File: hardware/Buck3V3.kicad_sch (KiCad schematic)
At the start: 10 parts, among them U301 AP63203WU

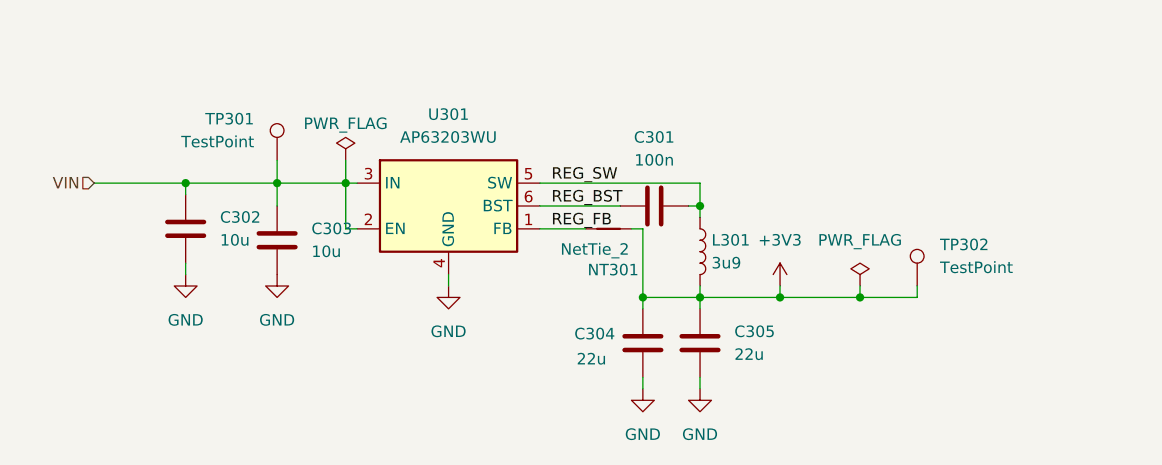
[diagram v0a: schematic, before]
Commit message: Optimized BOM and added netties
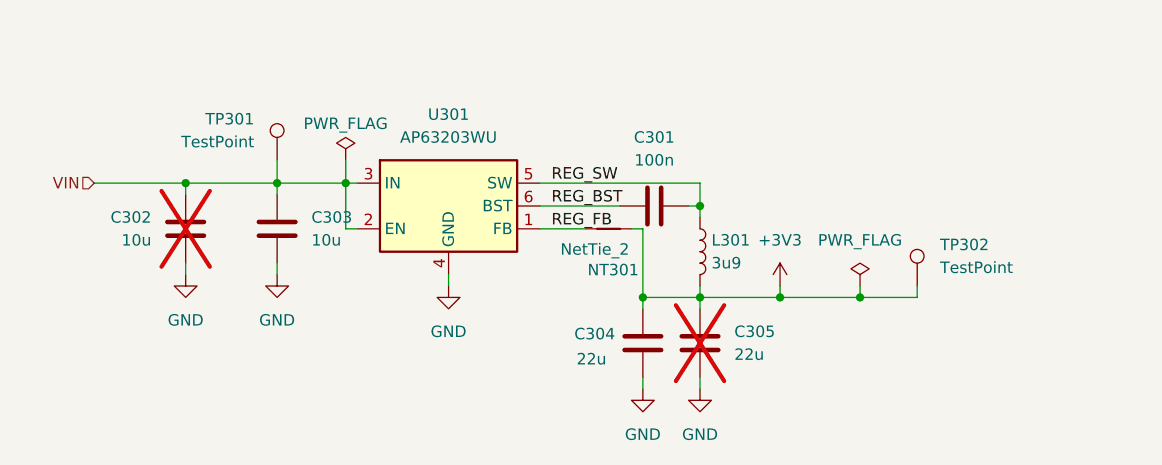
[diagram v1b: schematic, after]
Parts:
- C302, C305: now not fitted
- NT301: footprint rise:NETTIE_0.3mm -> glowbuck:NETTIE_0.3mm
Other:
- moved on the sheet: C303
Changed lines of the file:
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@@
 	(wire
 		(pts
-			(xy 53.34 48.26) (xy 53.34 45.72)
+			(xy 53.34 46.99) (xy 53.34 45.72)
 		)
 		(stroke
@@
 		(pts
 			(xy 118.11 58.42) (xy 118.11 57.15)
+		)
+		(stroke
+			(width 0)
+			(type default)
+		)
+	)
+	(wire
+		(pts
+			(xy 53.34 54.61) (xy 53.34 55.88)
 		)
 		(stroke
@@
 		(in_bom yes)
 		(on_board yes)
-		(dnp no)
+		(dnp yes)
 		(fields_autoplaced yes)
 		(property "Reference" "C302"
-			(at 46.99 49.5299 0)
-			(effects
-				(font
-					(size 1.27 1.27)
-				)
-				(justify left)
+			(at 39.37 49.5299 0)
+			(effects
+				(font
+					(size 1.27 1.27)
+				)
+				(justify right)
 			)
 		)
 		(property "Value" "10u"
-			(at 46.99 52.0699 0)
-			(effects
-				(font
-					(size 1.27 1.27)
-				)
-				(justify left)
+			(at 39.37 52.0699 0)
+			(effects
+				(font
+					(size 1.27 1.27)
+				)
+				(justify right)
 			)
 		)
@@
 	(symbol
 		(lib_id "Device:C")
-		(at 53.34 52.07 180)
+		(at 53.34 50.8 180)
 		(unit 1)
 		(exclude_from_sim no)
@@
 		(fields_autoplaced yes)
 		(property "Reference" "C303"
-			(at 57.15 50.7999 0)
+			(at 57.15 49.5299 0)
 			(effects
 				(font
@@
 		)
 		(property "Value" "10u"
-			(at 57.15 53.3399 0)
+			(at 57.15 52.0699 0)
 			(effects
 				(font
@@
 		)
 		(property "Footprint" "Capacitor_SMD:C_1210_3225Metric_Pad1.33x2.70mm_HandSolder"
-			(at 52.3748 48.26 0)
+			(at 52.3748 46.99 0)
 			(effects
 				(font
@@
 		)
 		(property "Datasheet" "~"
-			(at 53.34 52.07 0)
+			(at 53.34 50.8 0)
 			(effects
 				(font
@@
 		)
 		(property "Description" "Unpolarized capacitor"
-			(at 53.34 52.07 0)
+			(at 53.34 50.8 0)
 			(effects
 				(font
@@
 		)
 		(property "Sim.Device" ""
-			(at 53.34 52.07 0)
+			(at 53.34 50.8 0)
 			(effects
 				(font
@@
 		)
 		(property "Sim.Type" ""
-			(at 53.34 52.07 0)
+			(at 53.34 50.8 0)
 			(effects
 				(font
@@
 		)
 		(property "MouserNumber" "187-CL32B106KBJNNNE"
-			(at 53.34 52.07 0)
+			(at 53.34 50.8 0)
 			(effects
 				(font
@@
 		)
 		(property "OrderLink" ""
-			(at 53.34 52.07 0)
+			(at 53.34 50.8 0)
 			(effects
 				(font
@@
 		)
 		(property "Qty" ""
-			(at 53.34 52.07 0)
+			(at 53.34 50.8 0)
 			(effects
 				(font
@@
 		(in_bom yes)
 		(on_board yes)
-		(dnp no)
+		(dnp yes)
 		(fields_autoplaced yes)
 		(property "Reference" "C305"
@@
 			)
 		)
-		(property "Footprint" "rise:NETTIE_0.3mm"
+		(property "Footprint" "glowbuck:NETTIE_0.3mm"
 			(at 90.17 50.8 0)
 			(effects

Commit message: Changed footprints to non hand solder option
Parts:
- C301: footprint Capacitor_SMD:C_0603_1608Metric_Pad1.08x0.95mm_HandSolder -> Capacitor_SMD:C_0603_1608Metric
- C302, C303: footprint Capacitor_SMD:C_1210_3225Metric_Pad1.33x2.70mm_HandSolder -> Capacitor_SMD:C_1210_3225Metric
- C304, C305: footprint Capacitor_SMD:C_0805_2012Metric_Pad1.18x1.45mm_HandSolder -> Capacitor_SMD:C_0805_2012Metric
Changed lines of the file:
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@@
 			)
 		)
-		(property "Footprint" "Capacitor_SMD:C_1210_3225Metric_Pad1.33x2.70mm_HandSolder"
+		(property "Footprint" "Capacitor_SMD:C_1210_3225Metric"
 			(at 44.1452 54.61 0)
 			(effects
@@
 			)
 		)
-		(property "Footprint" "Capacitor_SMD:C_1210_3225Metric_Pad1.33x2.70mm_HandSolder"
+		(property "Footprint" "Capacitor_SMD:C_1210_3225Metric"
 			(at 52.3748 46.99 0)
 			(effects
@@
 			)
 		)
-		(property "Footprint" "Capacitor_SMD:C_0603_1608Metric_Pad1.08x0.95mm_HandSolder"
+		(property "Footprint" "Capacitor_SMD:C_0603_1608Metric"
 			(at 99.06 47.2948 0)
 			(effects
@@
 			)
 		)
-		(property "Footprint" "Capacitor_SMD:C_0805_2012Metric_Pad1.18x1.45mm_HandSolder"
+		(property "Footprint" "Capacitor_SMD:C_0805_2012Metric"
 			(at 99.3648 59.69 0)
 			(effects
@@
 			)
 		)
-		(property "Footprint" "Capacitor_SMD:C_0805_2012Metric_Pad1.18x1.45mm_HandSolder"
+		(property "Footprint" "Capacitor_SMD:C_0805_2012Metric"
 			(at 93.0148 59.69 0)
 			(effects

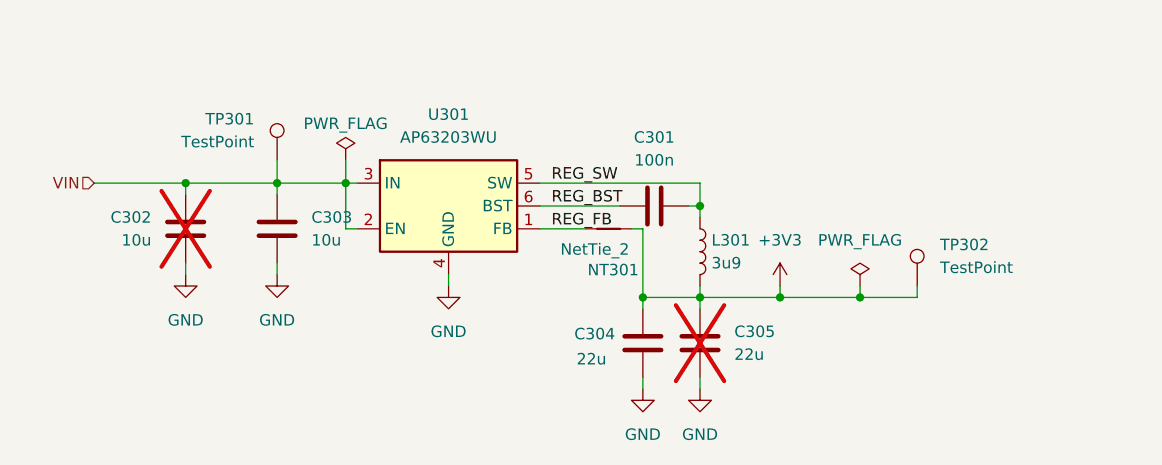
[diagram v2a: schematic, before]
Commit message: Colored nets and added optional current measurement
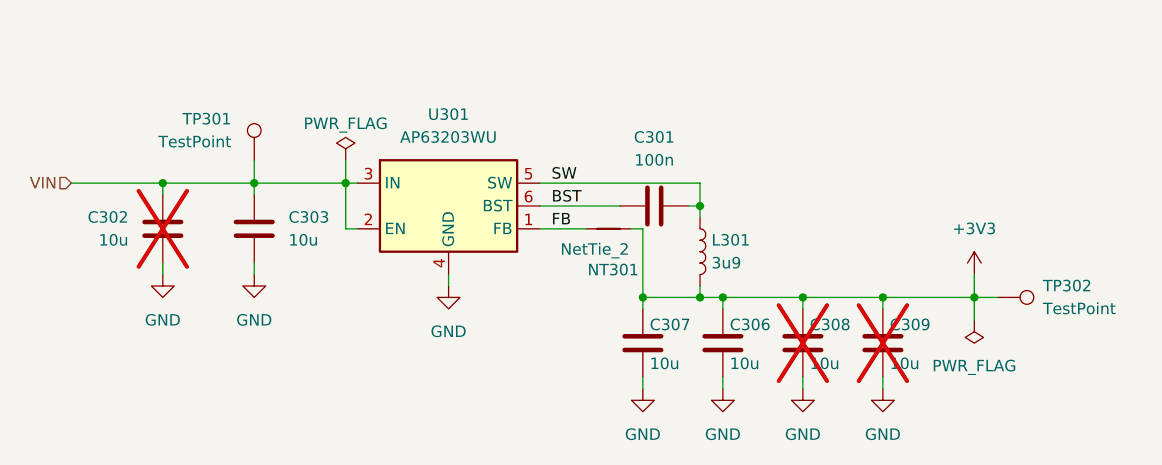
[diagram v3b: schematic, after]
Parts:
- removed C304, C305: 22u, Capacitor_SMD:C_0805_2012Metric, symbol Device:C
- added C306, C307, C308, C309: 10u, Capacitor_SMD:C_0603_1608Metric, symbol Device:C
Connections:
- net +3V3: now also C306.2, C307.2, C308.2, C309.2
- net GND: now also C306.1, C307.1, C308.1, C309.1
- net REG_BST renamed BST
- net REG_FB renamed FB
- net REG_SW renamed SW
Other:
- moved on the sheet: C302, C303, TP301, TP302

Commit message: Global labels, explanation texts, fix spring connector
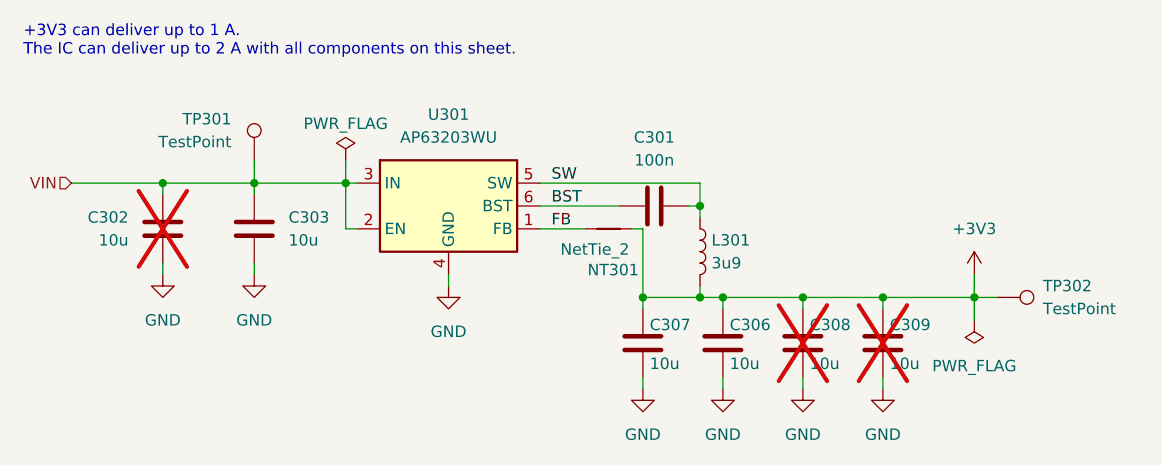
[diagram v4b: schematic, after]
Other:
- note added: "+3V3 can deliver up to 1 A. The IC can deliver up to 2 A with all components on this sheet."
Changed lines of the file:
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@@
 		(title "Glowbuck")
+	)
+	(text "+3V3 can deliver up to 1 A.\nThe IC can deliver up to 2 A with all components on this sheet."
+		(exclude_from_sim no)
+		(at 25.146 28.194 0)
+		(effects
+			(font
+				(size 1.27 1.27)
+			)
+			(justify left top)
+		)
 	)
 	(junction

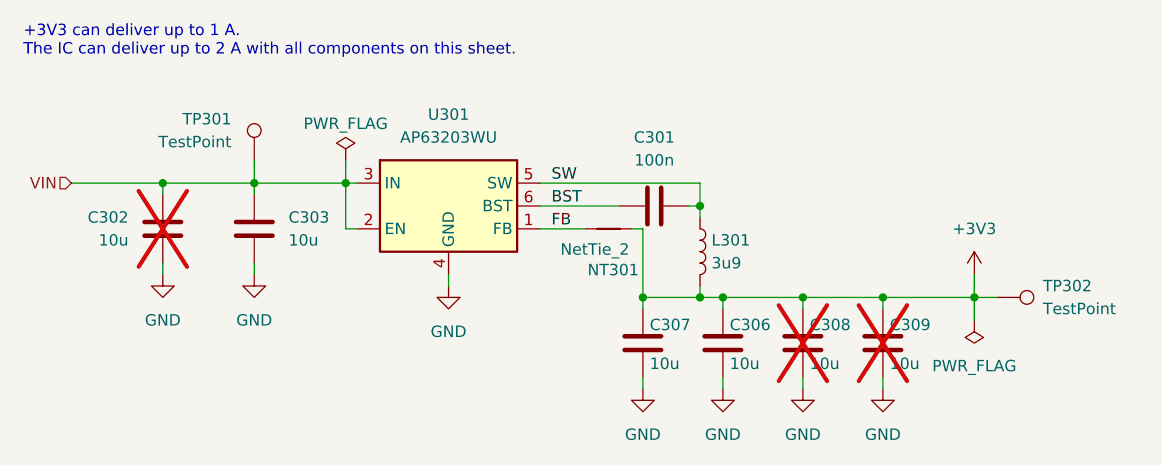
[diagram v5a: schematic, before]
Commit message: Layout in progress. I2C done
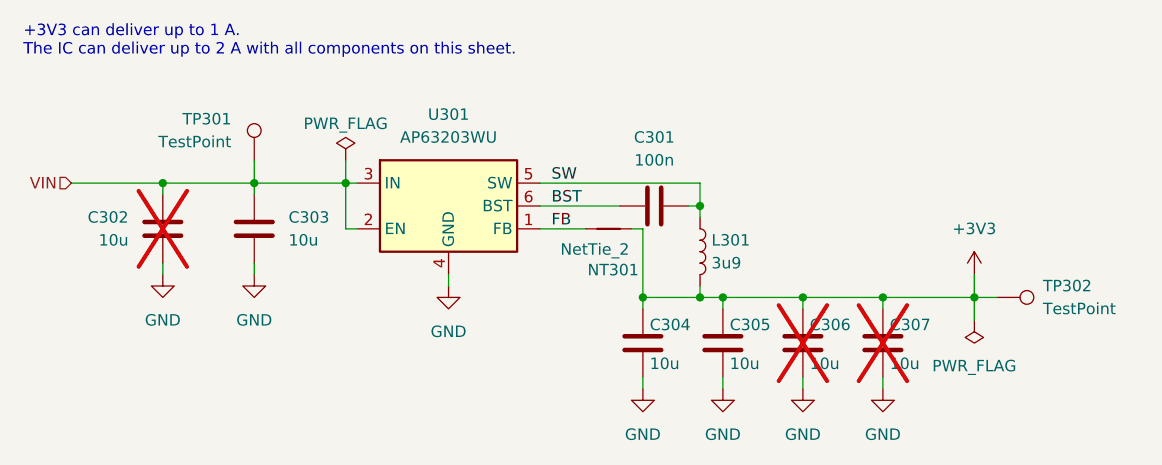
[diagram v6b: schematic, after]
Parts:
- renumbered C307 to C304, C306 to C305, C308 to C306, C309 to C307
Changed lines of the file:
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@@
 		(dnp no)
 		(fields_autoplaced yes)
-		(property "Reference" "#PWR0309"
+		(property "Reference" "#PWR0308"
 			(at 120.65 74.93 0)
 			(effects
@@
 			(project "glowbuck"
 				(path "/5c22e6dd-0c33-4422-b6db-bb3ef40a8534/4d6386b4-aba2-4d32-a7eb-dee692c742f8"
-					(reference "#PWR0309")
+					(reference "#PWR0308")
 					(unit 1)
 				)
@@
 		(exclude_from_sim no)
 		(in_bom yes)
-		(on_board yes)
+		(on_board no)
 		(dnp yes)
 		(fields_autoplaced yes)
@@
 		(on_board yes)
 		(dnp no)
-		(property "Reference" "C306"
+		(property "Reference" "C305"
 			(at 103.632 61.468 0)
 			(effects
@@
 			(project "glowbuck"
 				(path "/5c22e6dd-0c33-4422-b6db-bb3ef40a8534/4d6386b4-aba2-4d32-a7eb-dee692c742f8"
-					(reference "C306")
+					(reference "C305")
 					(unit 1)
 				)
@@
 		(exclude_from_sim no)
 		(in_bom yes)
-		(on_board yes)
+		(on_board no)
 		(dnp yes)
-		(property "Reference" "C308"
+		(property "Reference" "C306"
 			(at 112.522 61.468 0)
 			(effects
@@
 			(project "glowbuck"
 				(path "/5c22e6dd-0c33-4422-b6db-bb3ef40a8534/4d6386b4-aba2-4d32-a7eb-dee692c742f8"
-					(reference "C308")
+					(reference "C306")
 					(unit 1)
 				)
@@
 		(exclude_from_sim no)
 		(in_bom yes)
-		(on_board yes)
+		(on_board no)
 		(dnp yes)
-		(property "Reference" "C309"
+		(property "Reference" "C307"
 			(at 121.412 61.468 0)
 			(effects
@@
 			(project "glowbuck"
 				(path "/5c22e6dd-0c33-4422-b6db-bb3ef40a8534/4d6386b4-aba2-4d32-a7eb-dee692c742f8"
-					(reference "C309")
+					(reference "C307")
 					(unit 1)
 				)
@@
 		(dnp no)
 		(fields_autoplaced yes)
-		(property "Reference" "#PWR0307"
+		(property "Reference" "#PWR0306"
 			(at 102.87 74.93 0)
 			(effects
@@
 			(project "glowbuck"
 				(path "/5c22e6dd-0c33-4422-b6db-bb3ef40a8534/4d6386b4-aba2-4d32-a7eb-dee692c742f8"
-					(reference "#PWR0307")
+					(reference "#PWR0306")
 					(unit 1)
 				)
@@
 		(dnp no)
 		(fields_autoplaced yes)
-		(property "Reference" "#PWR0303"
+		(property "Reference" "#PWR0304"
 			(at 72.39 63.5 0)
 			(effects
@@
 			(project "glowbuck"
 				(path "/5c22e6dd-0c33-4422-b6db-bb3ef40a8534/4d6386b4-aba2-4d32-a7eb-dee692c742f8"
-					(reference "#PWR0303")
+					(reference "#PWR0304")
 					(unit 1)
 				)
@@
 		(dnp no)
 		(fields_autoplaced yes)
-		(property "Reference" "#PWR0308"
+		(property "Reference" "#PWR0307"
 			(at 111.76 74.93 0)
 			(effects
@@
 			(project "glowbuck"
 				(path "/5c22e6dd-0c33-4422-b6db-bb3ef40a8534/4d6386b4-aba2-4d32-a7eb-dee692c742f8"
-					(reference "#PWR0308")
+					(reference "#PWR0307")
 					(unit 1)
 				)
@@
 		(dnp no)
 		(fields_autoplaced yes)
-		(property "Reference" "#PWR0304"
+		(property "Reference" "#PWR0303"
 			(at 130.81 59.69 0)
 			(effects
@@
 			(project "glowbuck"
 				(path "/5c22e6dd-0c33-4422-b6db-bb3ef40a8534/4d6386b4-aba2-4d32-a7eb-dee692c742f8"
-					(reference "#PWR0304")
+					(reference "#PWR0303")
 					(unit 1)
 				)
@@
 		(on_board yes)
 		(dnp no)
-		(property "Reference" "C307"
+		(property "Reference" "C304"
 			(at 94.742 61.468 0)
 			(effects
@@
 			(project "glowbuck"
 				(path "/5c22e6dd-0c33-4422-b6db-bb3ef40a8534/4d6386b4-aba2-4d32-a7eb-dee692c742f8"
-					(reference "C307")
-					(unit 1)
-				)
+					(reference "C304")
+					(unit 1)
+				)

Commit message: Added ManufacturerNumber for every item and fixed bom errors
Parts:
- C301: ManufacturerNumber (none) -> CL10B104KB8WPND
- C302, C303: ManufacturerNumber (none) -> CL32B106KBJNNNE
- C304, C305, C306, C307: ManufacturerNumber (none) -> CL10A106MA8NRNC
- L301: ManufacturerNumber (none) -> SRR7045-3R9M
- U301: ManufacturerNumber (none) -> AP63203WU-7
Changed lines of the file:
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@@
+			)
+		)
+		(property "ManufacturerNumber" "CL32B106KBJNNNE"
+			(at 40.64 50.8 0)
+			(effects
+				(font
+					(size 1.27 1.27)
+				)
+				(hide yes)
 			)
 		)
@@
 		)
 		(property "Part" ""
+			(at 102.87 63.5 0)
+			(effects
+				(font
+					(size 1.27 1.27)
+				)
+				(hide yes)
+			)
+		)
+		(property "ManufacturerNumber" "CL10A106MA8NRNC"
 			(at 102.87 63.5 0)
 			(effects
@@
 			)
 		)
+		(property "ManufacturerNumber" "CL32B106KBJNNNE"
+			(at 50.8 50.8 0)
+			(effects
+				(font
+					(size 1.27 1.27)
+				)
+				(hide yes)
+			)
+		)
 		(pin "2"
 		)
@@
 			)
 		)
+		(property "ManufacturerNumber" "CL10A106MA8NRNC"
+			(at 111.76 63.5 0)
+			(effects
+				(font
+					(size 1.27 1.27)
+				)
+				(hide yes)
+			)
+		)
 		(pin "2"
 		)
@@
 		)
 		(property "Part" ""
+			(at 120.65 63.5 0)
+			(effects
+				(font
+					(size 1.27 1.27)
+				)
+				(hide yes)
+			)
+		)
+		(property "ManufacturerNumber" "CL10A106MA8NRNC"
 			(at 120.65 63.5 0)
 			(effects
@@
 			)
 		)
+		(property "ManufacturerNumber" "AP63203WU-7"
+			(at 72.39 48.26 0)
+			(effects
+				(font
+					(size 1.27 1.27)
+				)
+				(hide yes)
+			)
+		)
 		(pin "4"
 		)
@@
 		)
 		(property "Part" ""
+			(at 100.33 53.34 0)
+			(effects
+				(font
+					(size 1.27 1.27)
+				)
+				(hide yes)
+			)
+		)
+		(property "ManufacturerNumber" "SRR7045-3R9M"
 			(at 100.33 53.34 0)
 			(effects
@@
 			)
 		)
+		(property "ManufacturerNumber" "CL10B104KB8WPND"
+			(at 95.25 48.26 90)
+			(effects
+				(font
+					(size 1.27 1.27)
+				)
+				(hide yes)
+			)
+		)
 		(pin "2"
 		)
@@
 			(at 93.98 63.5 0)
 			(effects
+				(font
+					(size 1.27 1.27)
+				)
+				(hide yes)
+			)
+		)
+		(property "ManufacturerNumber" "CL10A106MA8NRNC"
+			(at 93.98 63.5 0)
+			(effects
